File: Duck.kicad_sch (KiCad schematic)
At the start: 34 parts, among them J1 KICK, J2 Aud IN, J3 OUT, J4 EurorackPower, Q1 2N3906, U3 VTL5C, U4 TL084

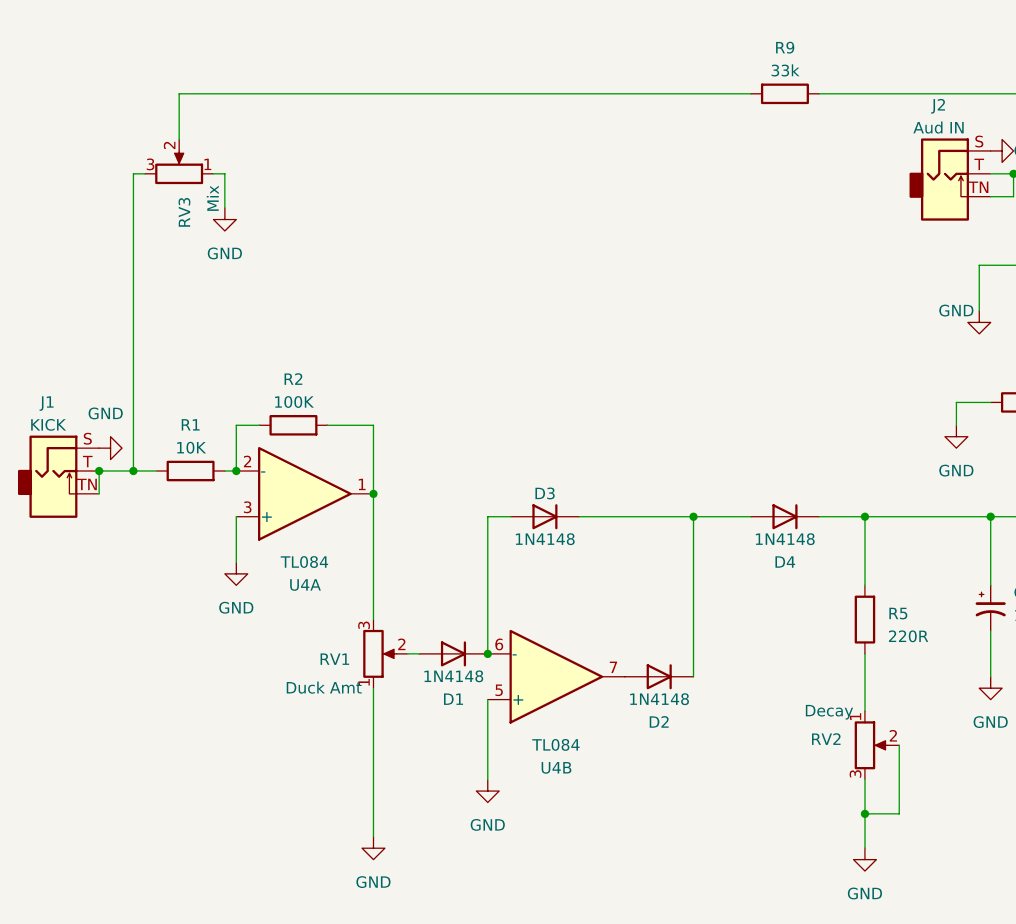
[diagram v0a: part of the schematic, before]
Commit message: Pot values added to schem and board
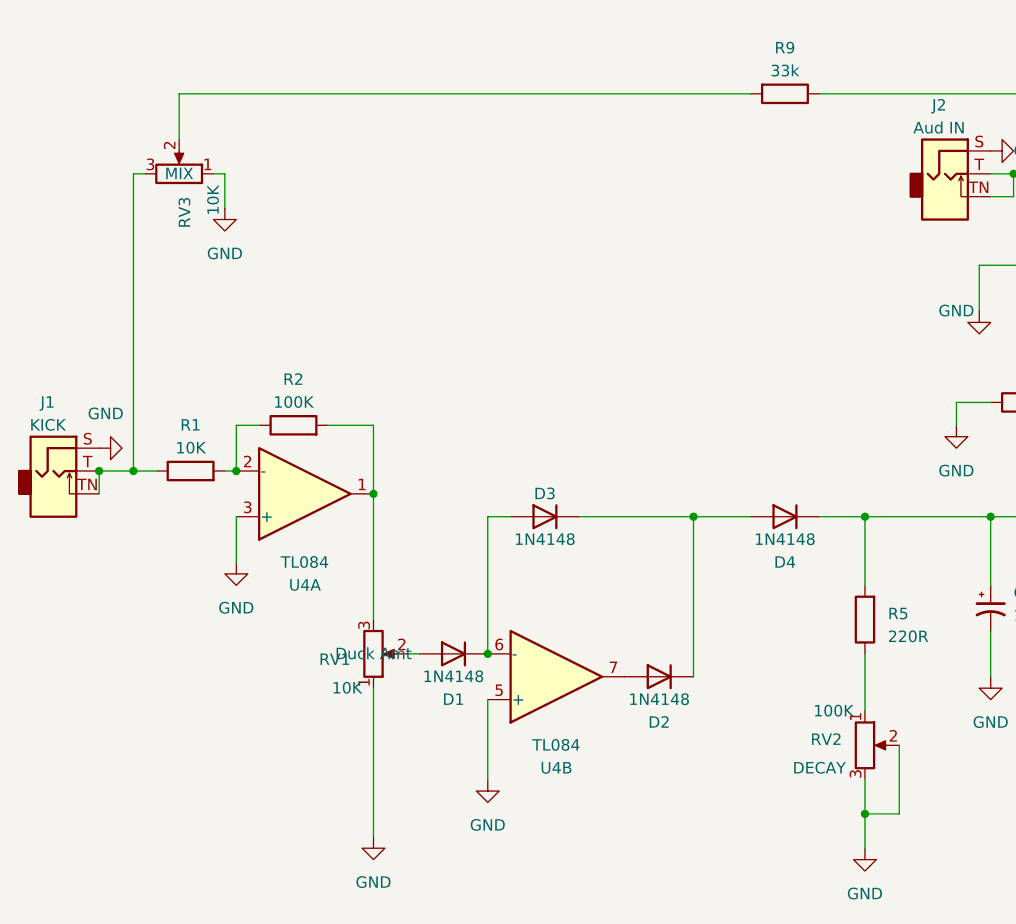
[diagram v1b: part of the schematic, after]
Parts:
- RV1: value Duck Amt -> 10K; NOTE (none) -> Duck Amt
- RV2: value Decay -> 100K; NOTE (none) -> DECAY; result DECAY -> (none)
- RV3: value Mix -> 10K; NOTE (none) -> MIX; result MIX -> (none)
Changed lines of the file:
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@@
       (effects (font (size 1.27 1.27)) (justify right))
     )
-    (property "Value" "Duck Amt" (at 78.74 137.16 0)
+    (property "Value" "10K" (at 78.74 137.16 0)
       (effects (font (size 1.27 1.27)) (justify right))
     )
@@
     (property "Datasheet" "~" (at 80.01 133.35 0)
       (effects (font (size 1.27 1.27)) hide)
+    )
+    (property "NOTE" "Duck Amt" (at 80.01 133.35 0)
+      (effects (font (size 1.27 1.27)))
     )
     (pin "1")
@@
       (effects (font (size 1.27 1.27)) (justify right))
     )
-    (property "Value" "Mix" (at 62.23 81.28 0)
+    (property "Value" "10K" (at 62.23 81.28 0)
       (effects (font (size 1.27 1.27)) (justify right))
     )
@@
       (effects (font (size 1.27 1.27)) hide)
     )
-    (property "result" "MIX" (at 58.42 80.01 90)
-      (effects (font (size 1.27 1.27)) hide)
+    (property "NOTE" "MIX" (at 58.42 80.01 90)
+      (effects (font (size 1.27 1.27)))
     )
     (pin "1")
@@
       (effects (font (size 1.27 1.27)) (justify right))
     )
-    (property "Value" "Decay" (at 133.35 139.7 0)
+    (property "Value" "100K" (at 133.35 139.7 0)
       (effects (font (size 1.27 1.27)) (justify right))
     )
@@
       (effects (font (size 1.27 1.27)) hide)
     )
-    (property "result" "DECAY" (at 129.54 146.05 0)
-      (effects (font (size 1.27 1.27)) hide)
-    )
-    (pin "1")
+    (property "NOTE" "DECAY" (at 129.54 146.05 0)
+      (effects (font (size 1.27 1.27)))
+    )
+    (pin "1")
